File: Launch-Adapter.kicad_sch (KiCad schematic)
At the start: 0 parts

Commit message: Первая версия в производство
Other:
- added sheet Relay_Control (Relay_Control.kicad_sch)
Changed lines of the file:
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@@
+    )
+  )
+  (sheet (at 54.61 17.272) (size 22.225 17.78) (fields_autoplaced)
+    (stroke (width 0.1524) (type solid) (color 0 0 0 0))
+    (fill (color 0 0 0 0.0000))
+    (property "Sheet name" "Relay_Control" (id 0) (at 54.61 16.5604 0)
+      (effects (font (size 1.27 1.27)) (justify left bottom))
+    )
+    (property "Sheet file" "Relay_Control.kicad_sch" (id 1) (at 54.61 35.6366 0)
+      (effects (font (size 1.27 1.27)) (justify left top))
     )
   )
@@
     (path "/9700aaad-e8e8-484b-ae67-8cfb79e9bec7" (page "7"))
     (path "/8ded4ace-7a7c-4cba-ad2c-06c1a78ed04c" (page "8"))
+    (path "/7ed26b9a-ae35-4590-a040-063aa8adf3ad" (page "9"))
   )
   (symbol_instances
@@
       (reference "#PWR019") (unit 1) (value "+5VD") (footprint "")
     )
+    (path "/fb199889-8150-455c-81a1-ac716a239708/745894e0-ef65-49d0-abe3-e929689797fa"
+      (reference "#PWR020") (unit 1) (value "GNDD") (footprint "")
+    )
+    (path "/fb199889-8150-455c-81a1-ac716a239708/4610f617-7c51-48e6-bdf1-f30ac4bd349a"
+      (reference "#PWR021") (unit 1) (value "GNDD") (footprint "")
+    )
+    (path "/fb199889-8150-455c-81a1-ac716a239708/6d959cda-b09c-4b57-ad32-e44a90326ec5"
+      (reference "#PWR022") (unit 1) (value "GNDD") (footprint "")
+    )
+    (path "/7ed26b9a-ae35-4590-a040-063aa8adf3ad/53721a6f-3d0f-4f28-b950-946cb264f90f"
+      (reference "#PWR023") (unit 1) (value "+3.3V") (footprint "")
+    )
     (path "/fb199889-8150-455c-81a1-ac716a239708/2218af71-4653-4b11-8c41-a17dd26557ff"
       (reference "#PWR024") (unit 1) (value "GND2") (footprint "")
@@
       (reference "#PWR025") (unit 1) (value "GND") (footprint "")
     )
+    (path "/7ed26b9a-ae35-4590-a040-063aa8adf3ad/7cb0ed78-403e-4fb2-9c4c-619d440880b5"
+      (reference "#PWR026") (unit 1) (value "GND") (footprint "")
+    )
+    (path "/692023e0-e330-4644-b46c-568e5e70027d/c235f987-e4bd-43bf-bb0f-ac1c07fd0d01"
+      (reference "#PWR027") (unit 1) (value "GND") (footprint "")
+    )
+    (path "/692023e0-e330-4644-b46c-568e5e70027d/c3c98697-4aae-4816-b13b-414356ae58bc"
+      (reference "#PWR028") (unit 1) (value "GND") (footprint "")
+    )
+    (path "/692023e0-e330-4644-b46c-568e5e70027d/fe4ea9de-6dd8-4285-b334-3776a4878cfc"
+      (reference "#PWR029") (unit 1) (value "GND") (footprint "")
+    )
     (path "/692023e0-e330-4644-b46c-568e5e70027d/4d5ec5c8-9ba2-42e1-b461-ae7bc1c590cf"
       (reference "#PWR030") (unit 1) (value "GND") (footprint "")
@@
       (reference "#PWR031") (unit 1) (value "GND") (footprint "")
     )
+    (path "/7ed26b9a-ae35-4590-a040-063aa8adf3ad/080aca92-8eff-4e94-98df-45c67e274419"
+      (reference "#PWR032") (unit 1) (value "GND") (footprint "")
+    )
+    (path "/7ed26b9a-ae35-4590-a040-063aa8adf3ad/ea71e857-6dc0-476a-bf19-158677ca97b5"
+      (reference "#PWR033") (unit 1) (value "+15V") (footprint "")
+    )
+    (path "/7ed26b9a-ae35-4590-a040-063aa8adf3ad/cc971596-ff3f-4ca9-9e0f-0d2c72e70c57"
+      (reference "#PWR034") (unit 1) (value "GND") (footprint "")
+    )
+    (path "/9700aaad-e8e8-484b-ae67-8cfb79e9bec7/a21be73b-ad43-45ea-86ce-d13ce1d43e99"
+      (reference "#PWR035") (unit 1) (value "GND") (footprint "")
+    )
     (path "/692023e0-e330-4644-b46c-568e5e70027d/698d4464-34da-4a32-bc65-71f0e47526c6"
       (reference "#PWR036") (unit 1) (value "GND") (footprint "")
@@
       (reference "#PWR037") (unit 1) (value "GND") (footprint "")
     )
+    (path "/9700aaad-e8e8-484b-ae67-8cfb79e9bec7/aac3218c-58ac-4a6b-822d-c9a2531d2d80"
+      (reference "#PWR038") (unit 1) (value "GND") (footprint "")
+    )
     (path "/692023e0-e330-4644-b46c-568e5e70027d/d0b91de0-8db2-4568-99d8-6a68ab6af3cd"
       (reference "#PWR040") (unit 1) (value "GND") (footprint "")
@@
       (reference "#PWR072") (unit 1) (value "GND") (footprint "")
     )
-    (path "/fb199889-8150-455c-81a1-ac716a239708/09828461-7ea9-4f20-a3e1-d781f3eae7f0"
-      (reference "#PWR073") (unit 1) (value "GND") (footprint "")
-    )
-    (path "/fb199889-8150-455c-81a1-ac716a239708/8ba9c48a-0b5a-47fc-afc5-262066d63971"
-      (reference "#PWR074") (unit 1) (value "GND") (footprint "")
-    )
     (path "/2e7a20af-2214-4346-958e-b610b512a398/49270af2-9c6a-419a-bfc2-354037c212f1"
       (reference "#PWR0101") (unit 1) (value "GND") (footprint "")
@@
       (reference "C25") (unit 1) (value "100n") (footprint "Capacitor_SMD:C_0805_2012Metric_Pad1.18x1.45mm_HandSolder")
     )
+    (path "/7ed26b9a-ae35-4590-a040-063aa8adf3ad/08b50101-c019-4645-9b55-5806a47d4be2"
+      (reference "D1") (unit 1) (value "PVT412LSPBF") (footprint "Package_DIP:DIP-6_W8.89mm_SMDSocket_LongPads")
+    )
+    (path "/7ed26b9a-ae35-4590-a040-063aa8adf3ad/bf0f2adb-7907-4752-af42-2f9a2ed85d8b"
+      (reference "D2") (unit 1) (value "D_Small") (footprint "Diode_SMD:D_SOD-323F")
+    )
     (path "/cf7391a2-da21-4780-a699-e488bf23f530/8c563aa8-9f1c-4f9d-bb87-4701aea6754c"
       (reference "D4") (unit 1) (value "LED_Small") (footprint "LED_SMD:LED_0805_2012Metric_Pad1.15x1.40mm_HandSolder")
@@
       (reference "J5") (unit 1) (value "Driver") (footprint "Connector_IDC:IDC-Header_2x07-1MP_P2.54mm_Latch_Vertical")
     )
-    (path "/8ded4ace-7a7c-4cba-ad2c-06c1a78ed04c/9b39bc23-8689-44f8-84b5-aef8378d7fdb"
-      (reference "J6") (unit 1) (value "Measurements") (footprint "Connector_IDC:IDC-Header_2x05_P2.54mm_Vertical")
+    (path "/692023e0-e330-4644-b46c-568e5e70027d/eac0966b-248f-458a-98d9-ec9107f5bdc2"
+      (reference "J6") (unit 1) (value "Voltage measure") (footprint "Connector_Molex:Molex_Micro-Fit_3.0_43045-0400_2x02_P3.00mm_Horizontal")
     )
     (path "/2e7a20af-2214-4346-958e-b610b512a398/5aeb1e78-7ed8-446f-a1fa-e72019642e8e"
@@
       (reference "J10") (unit 1) (value "+5V_CAN") (footprint "Connector_Molex:Molex_Micro-Fit_3.0_43045-0400_2x02_P3.00mm_Horizontal")
     )
-    (path "/8ded4ace-7a7c-4cba-ad2c-06c1a78ed04c/724372e0-5b74-4c53-9cf9-e45fa4a6f364"
-      (reference "J11") (unit 1) (value "Input") (footprint "Connector_Molex:Molex_Micro-Fit_3.0_43045-0600_2x03_P3.00mm_Horizontal")
+    (path "/fb199889-8150-455c-81a1-ac716a239708/56e1f11d-cc8e-4fae-b028-f73e489ecda7"
+      (reference "J11") (unit 1) (value "Interfaces") (footprint "Connector_Molex:Molex_Micro-Fit_3.0_43045-0800_2x04_P3.00mm_Horizontal")
+    )
+    (path "/692023e0-e330-4644-b46c-568e5e70027d/cdcfcb5e-d6bb-4686-9fa7-b194d3eaa510"
+      (reference "J12") (unit 1) (value "Current Measure") (footprint "Connector_Molex:Molex_Micro-Fit_3.0_43045-0400_2x02_P3.00mm_Horizontal")
+    )
+    (path "/7ed26b9a-ae35-4590-a040-063aa8adf3ad/5b6e317d-19de-4a99-b35a-a856709a0b17"
+      (reference "J13") (unit 1) (value "Current Measure") (footprint "Connector_Molex:Molex_Micro-Fit_3.0_43045-0400_2x02_P3.00mm_Horizontal")
+    )
+    (path "/7ed26b9a-ae35-4590-a040-063aa8adf3ad/4ec09d12-cc8c-471c-9599-ed071ddff80f"
+      (reference "Q1") (unit 1) (value "BC817") (footprint "Package_TO_SOT_SMD:SOT-23")
     )
     (path "/fb199889-8150-455c-81a1-ac716a239708/61aaa715-f6c3-453d-8f5c-8c66586b768c"
@@
       (reference "R15") (unit 1) (value "49.9") (footprint "Resistor_SMD:R_0805_2012Metric_Pad1.20x1.40mm_HandSolder")
     )
+    (path "/7ed26b9a-ae35-4590-a040-063aa8adf3ad/28b1bd38-3ec2-4c42-ac89-4d1ee4106fdf"
+      (reference "R16") (unit 1) (value "4.7k") (footprint "Resistor_SMD:R_0805_2012Metric_Pad1.20x1.40mm_HandSolder")
+    )
     (path "/cf7391a2-da21-4780-a699-e488bf23f530/6c5e8f09-5b4d-4cf2-a42f-c27a9edbe39e"
       (reference "R17") (unit 1) (value "1.5k") (footprint "Resistor_SMD:R_0805_2012Metric_Pad1.20x1.40mm_HandSolder")
@@
       (reference "R38") (unit 1) (value "0") (footprint "Resistor_SMD:R_0805_2012Metric_Pad1.20x1.40mm_HandSolder")
     )
-    (path "/8b70914e-1173-4534-a582-e2bced939c13/d8a251c5-e75b-4a11-b07d-ec6c9792d8d5"
-      (reference "R41") (unit 1) (value "0") (footprint "Resistor_SMD:R_0805_2012Metric_Pad1.20x1.40mm_HandSolder")
-    )
-    (path "/8b70914e-1173-4534-a582-e2bced939c13/638d3c5d-0e0a-40ca-8972-60bbd8026d81"
-      (reference "R42") (unit 1) (value "0") (footprint "Resistor_SMD:R_0805_2012Metric_Pad1.20x1.40mm_HandSolder")
+    (path "/7ed26b9a-ae35-4590-a040-063aa8adf3ad/e84cd9b4-b67a-4278-bb4c-47e9eaf45741"
+      (reference "R39") (unit 1) (value "10k") (footprint "Resistor_SMD:R_0805_2012Metric_Pad1.20x1.40mm_HandSolder")
+    )
+    (path "/7ed26b9a-ae35-4590-a040-063aa8adf3ad/d63cce10-7b63-4226-a96e-b404a06697a3"
+      (reference "R40") (unit 1) (value "220") (footprint "Resistor_SMD:R_0805_2012Metric_Pad1.20x1.40mm_HandSolder")
+    )
+    (path "/7ed26b9a-ae35-4590-a040-063aa8adf3ad/33805502-1684-44c3-9dd5-d32c88a89b36"
+      (reference "R41") (unit 1) (value "60") (footprint "Resistor_SMD:R_0805_2012Metric_Pad1.20x1.40mm_HandSolder")
+    )
+    (path "/9700aaad-e8e8-484b-ae67-8cfb79e9bec7/0836ce24-cc12-402a-bd21-88aeb4e49c42"
+      (reference "R42") (unit 1) (value "10k") (footprint "Resistor_SMD:R_0805_2012Metric_Pad1.20x1.40mm_HandSolder")
     )
     (path "/8b70914e-1173-4534-a582-e2bced939c13/ecbbc6f9-0a45-4ffd-afde-6b53b220970a"
@@
       (reference "R46") (unit 1) (value "0") (footprint "Resistor_SMD:R_0805_2012Metric_Pad1.20x1.40mm_HandSolder")
     )
+    (path "/9700aaad-e8e8-484b-ae67-8cfb79e9bec7/06764674-c69f-48d2-ab72-b234dd1757f5"
+      (reference "R47") (unit 1) (value "10k") (footprint "Resistor_SMD:R_0805_2012Metric_Pad1.20x1.40mm_HandSolder")
+    )
     (path "/fb199889-8150-455c-81a1-ac716a239708/93913930-e7d9-48e3-99b0-b408d466fbc3"

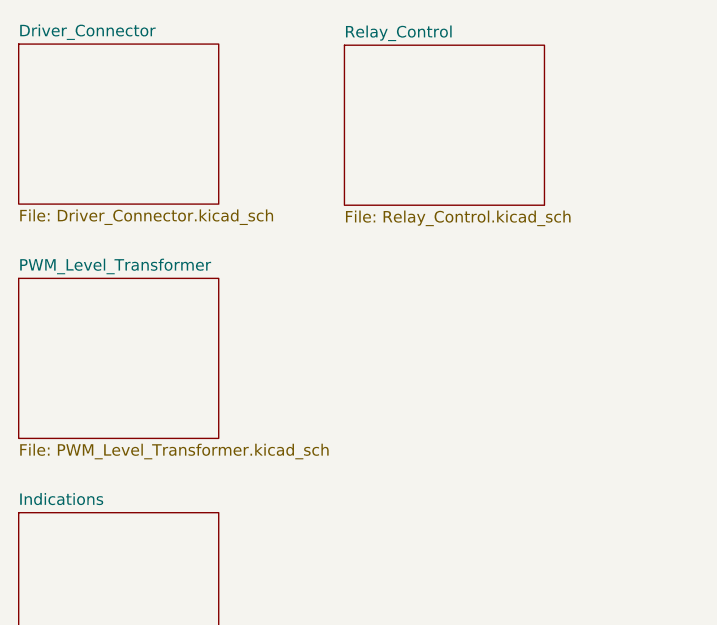
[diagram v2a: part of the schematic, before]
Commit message: Добавил температуру, убрал подтяжки RS-485, заменил ШИМ на дифференциальный сигнал, добавил земли RS-485
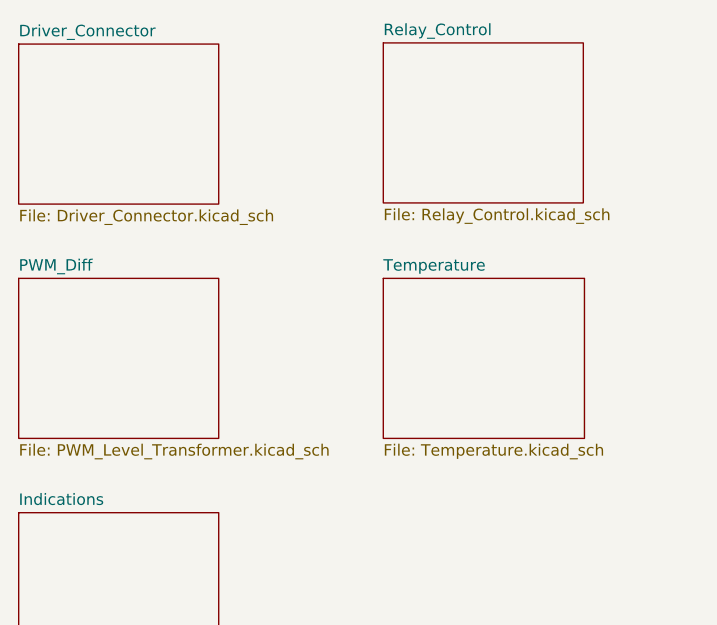
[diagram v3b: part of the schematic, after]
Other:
- sheet PWM_Level_Transformer renamed PWM_Diff
- added sheet Temperature (Temperature.kicad_sch)
